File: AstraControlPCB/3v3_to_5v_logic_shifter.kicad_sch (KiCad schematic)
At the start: 16 parts, among them U6 TXB0104PWR

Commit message: Update wks file
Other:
- company: (none) -> LiveAstra Technologies
- title: 3V3 to 5V Logic Shifter -> AstraControl - Root
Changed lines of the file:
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@@
 	(paper "A4")
 	(title_block
-		(title "3V3 to 5V Logic Shifter")
+		(title "AstraControl - Root")
+		(date "2024-08-26")
+		(rev "A")
+		(company "LiveAstra Technologies")
 	)
 	(junction

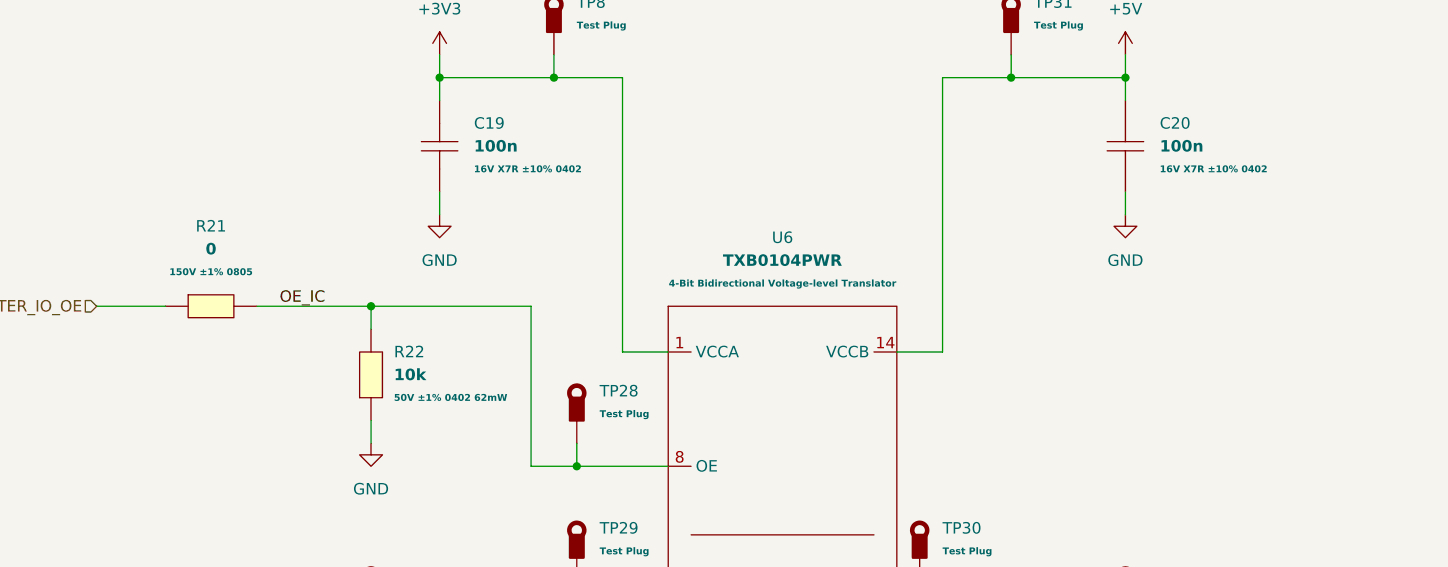
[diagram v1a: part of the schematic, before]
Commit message: Remove plus minus symbol
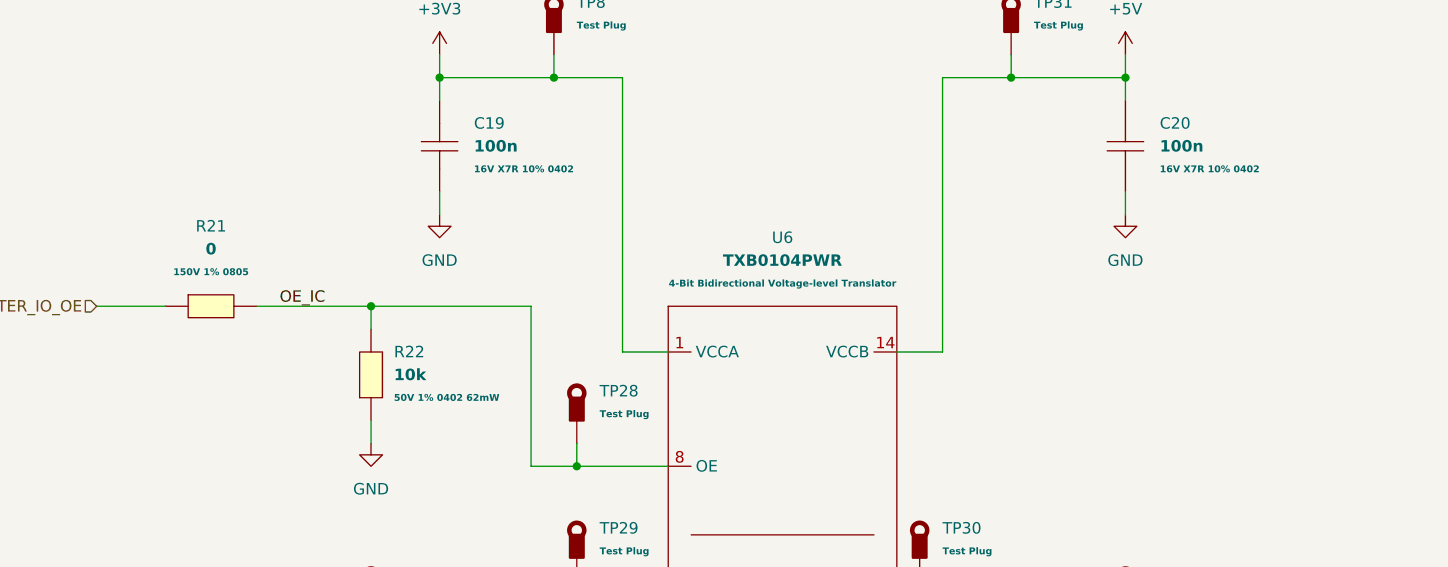
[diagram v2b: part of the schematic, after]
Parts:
- C19, C20: Extra Values 16V X7R ±10% 0402 -> 16V X7R 10% 0402
- R21: Extra Values 150V ±1% 0805 -> 150V 1% 0805
- R22: Extra Values 50V ±1% 0402 62mW -> 50V 1% 0402 62mW
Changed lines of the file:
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@@
 		(dnp no)
 		(fields_autoplaced yes)
-		(property "Reference" "#PWR059"
+		(property "Reference" "#PWR59"
 			(at 190.5 72.39 0)
 			(effects
@@
 			(project "AstraControl"
 				(path "/9a751838-dce8-4d69-8a02-736625ac74e7/0db21d8e-3390-4d67-877f-0e5d98e37848/12d48f68-9e8c-4210-a297-afac62bc105d"
-					(reference "#PWR059")
+					(reference "#PWR59")
 					(unit 1)
 				)
@@
 			)
 		)
-		(property "Extra Value" ""
-			(at 129.54 91.44 0)
-			(effects
-				(font
-					(size 1.27 1.27)
-				)
-				(hide yes)
-			)
-		)
 		(pin "1"
 		)
@@
 			)
 		)
-		(property "Extra Values" "50V ±1% 0402 62mW"
+		(property "Extra Values" "50V 1% 0402 62mW"
 			(at 109.22 86.3599 90)
 			(effects
@@
 				)
 				(justify right)
-			)
-		)
-		(property "Extra Value" ""
-			(at 106.68 83.82 0)
-			(effects
-				(font
-					(size 1.27 1.27)
-				)
-				(hide yes)
 			)
 		)
@@
 		(dnp no)
 		(fields_autoplaced yes)
-		(property "Reference" "#PWR054"
+		(property "Reference" "#PWR54"
 			(at 106.68 97.79 0)
 			(effects
@@
 			(project "AstraControl"
 				(path "/9a751838-dce8-4d69-8a02-736625ac74e7/0db21d8e-3390-4d67-877f-0e5d98e37848/12d48f68-9e8c-4210-a297-afac62bc105d"
-					(reference "#PWR054")
+					(reference "#PWR54")
 					(unit 1)
 				)
@@
 		(dnp no)
 		(fields_autoplaced yes)
-		(property "Reference" "#PWR058"
+		(property "Reference" "#PWR58"
 			(at 190.5 52.07 0)
 			(effects
@@
 			(project "AstraControl"
 				(path "/9a751838-dce8-4d69-8a02-736625ac74e7/0db21d8e-3390-4d67-877f-0e5d98e37848/12d48f68-9e8c-4210-a297-afac62bc105d"
-					(reference "#PWR058")
+					(reference "#PWR58")
 					(unit 1)
 				)
@@
 		(dnp no)
 		(fields_autoplaced yes)
-		(property "Reference" "#PWR055"
+		(property "Reference" "#PWR55"
 			(at 114.3 52.07 0)
 			(effects
@@
 			(project "AstraControl"
 				(path "/9a751838-dce8-4d69-8a02-736625ac74e7/0db21d8e-3390-4d67-877f-0e5d98e37848/12d48f68-9e8c-4210-a297-afac62bc105d"
-					(reference "#PWR055")
+					(reference "#PWR55")
 					(unit 1)
 				)
@@
 			)
 		)
-		(property "Extra Value" ""
-			(at 129.54 106.68 0)
-			(effects
-				(font
-					(size 1.27 1.27)
-				)
-				(hide yes)
-			)
-		)
 		(pin "1"
 		)
@@
 			)
 		)
-		(property "Extra Value" ""
-			(at 81.28 116.84 0)
-			(effects
-				(font
-					(size 1.27 1.27)
-				)
-				(hide yes)
-			)
-		)
 		(pin "1"
 		)
@@
 			)
 		)
-		(property "Extra Value" ""
-			(at 152.4 88.9 0)
-			(effects
-				(font
-					(size 1.27 1.27)
-				)
-				(hide yes)
-			)
-		)
 		(pin "5"
 		)
@@
 			)
 		)
-		(property "Extra Value" ""
-			(at 215.9 116.84 0)
-			(effects
-				(font
-					(size 1.27 1.27)
-				)
-				(hide yes)
-			)
-		)
 		(pin "1"
 		)
@@
 			)
 		)
-		(property "Extra Value" ""
-			(at 106.68 111.76 0)
-			(effects
-				(font
-					(size 1.27 1.27)
-				)
-				(hide yes)
-			)
-		)
 		(pin "1"
 		)
@@
 			)
 		)
-		(property "Extra Values" "150V ±1% 0805"
+		(property "Extra Values" "150V 1% 0805"
 			(at 88.9 72.39 0)
 			(effects
@@
 					(bold yes)
 				)
-			)
-		)
-		(property "Extra Value" ""
-			(at 88.9 76.2 0)
-			(effects
-				(font
-					(size 1.27 1.27)
-				)
-				(hide yes)
 			)
 		)
@@
 		(dnp no)
 		(fields_autoplaced yes)
-		(property "Reference" "#PWR056"
+		(property "Reference" "#PWR56"
 			(at 114.3 72.39 0)
 			(effects
@@
 			(project "AstraControl"
 				(path "/9a751838-dce8-4d69-8a02-736625ac74e7/0db21d8e-3390-4d67-877f-0e5d98e37848/12d48f68-9e8c-4210-a297-afac62bc105d"
-					(reference "#PWR056")
+					(reference "#PWR56")
 					(unit 1)
 				)
@@
 			)
 		)
-		(property "Extra Value" ""
-			(at 167.64 106.68 0)
-			(effects
-				(font
-					(size 1.27 1.27)
-				)
-				(hide yes)
-			)
-		)
 		(pin "1"
 		)
@@
 			)
 		)
-		(property "Extra Value" ""
-			(at 55.88 121.92 0)
-			(effects
-				(font
-					(size 1.27 1.27)
-				)
-				(hide yes)
-			)
-		)
 		(pin "1"
 		)
@@
 		(dnp no)
 		(fields_autoplaced yes)
-		(property "Reference" "#PWR057"
+		(property "Reference" "#PWR57"
 			(at 152.4 143.51 0)
 			(effects
@@
 			(project "AstraControl"
 				(path "/9a751838-dce8-4d69-8a02-736625ac74e7/0db21d8e-3390-4d67-877f-0e5d98e37848/12d48f68-9e8c-4210-a297-afac62bc105d"
-					(reference "#PWR057")
+					(reference "#PWR57")
 					(unit 1)
 				)
@@
 			)
 		)
-		(property "Extra Value" ""
-			(at 243.84 121.92 0)
-			(effects
-				(font
-					(size 1.27 1.27)
-				)
-				(hide yes)
-			)
-		)
 		(pin "1"
 		)
@@
 			)
 		)
-		(property "Extra Value" ""
-			(at 127 48.26 0)
-			(effects
-				(font
-					(size 1.27 1.27)
-				)
-				(hide yes)
-			)
-		)
 		(pin "1"
 		)
@@
 			)
 		)
-		(property "Extra Value" ""
-			(at 177.8 48.26 0)
-			(effects
-				(font
-					(size 1.27 1.27)
-				)
-				(hide yes)
-			)
-		)
 		(pin "1"
 		)
@@
 			)
 		)
-		(property "Extra Values" "16V X7R ±10% 0402"
+		(property "Extra Values" "16V X7R 10% 0402"
 			(at 118.11 60.9599 90)
 			(effects
@@
 				)
 				(justify right)
-			)
-		)
-		(property "Extra Value" ""
-			(at 114.3 58.42 0)
-			(effects
-				(font
-					(size 1.27 1.27)
-				)
-				(hide yes)
 			)
 		)
@@
 			)
 		)
-		(property "Extra Values" "16V X7R ±10% 0402"
+		(property "Extra Values" "16V X7R 10% 0402"
 			(at 194.31 60.9599 90)
 			(effects
@@
 				)
 				(justify right)
-			)
-		)
-		(property "Extra Value" ""
-			(at 190.5 58.42 0)
-			(effects
-				(font
-					(size 1.27 1.27)
-				)
-				(hide yes)
 			)
 		)
@@
 			)
 		)
-		(property "Extra Value" ""
-			(at 190.5 111.76 0)
-			(effects
-				(font
-					(size 1.27 1.27)
-				)
-				(hide yes)
-			)
-		)

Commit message: workflow
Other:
- note added: "3V3 to 5V Logic Shifter"
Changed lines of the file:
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@@
+		)
+	)
+	(text "3V3 to 5V Logic Shifter"
+		(exclude_from_sim no)
+		(at 19.05 25.4 0)
+		(effects
+			(font
+				(face "ING Me Headline")
+				(size 8 8)
+			)
+			(justify left top)
 		)
 	)
@@
 		(dnp no)
 		(fields_autoplaced yes)
-		(property "Reference" "#PWR59"
+		(property "Reference" "#PWR059"
 			(at 190.5 72.39 0)
 			(effects
@@
 			(project "AstraControl"
 				(path "/9a751838-dce8-4d69-8a02-736625ac74e7/0db21d8e-3390-4d67-877f-0e5d98e37848/12d48f68-9e8c-4210-a297-afac62bc105d"
-					(reference "#PWR59")
+					(reference "#PWR059")
 					(unit 1)
 				)
@@
 		(dnp no)
 		(fields_autoplaced yes)
-		(property "Reference" "#PWR54"
+		(property "Reference" "#PWR054"
 			(at 106.68 97.79 0)
 			(effects
@@
 			(project "AstraControl"
 				(path "/9a751838-dce8-4d69-8a02-736625ac74e7/0db21d8e-3390-4d67-877f-0e5d98e37848/12d48f68-9e8c-4210-a297-afac62bc105d"
-					(reference "#PWR54")
+					(reference "#PWR054")
 					(unit 1)
 				)
@@
 		(dnp no)
 		(fields_autoplaced yes)
-		(property "Reference" "#PWR58"
+		(property "Reference" "#PWR058"
 			(at 190.5 52.07 0)
 			(effects
@@
 			(project "AstraControl"
 				(path "/9a751838-dce8-4d69-8a02-736625ac74e7/0db21d8e-3390-4d67-877f-0e5d98e37848/12d48f68-9e8c-4210-a297-afac62bc105d"
-					(reference "#PWR58")
+					(reference "#PWR058")
 					(unit 1)
 				)
@@
 		(dnp no)
 		(fields_autoplaced yes)
-		(property "Reference" "#PWR55"
+		(property "Reference" "#PWR055"
 			(at 114.3 52.07 0)
 			(effects
@@
 			(project "AstraControl"
 				(path "/9a751838-dce8-4d69-8a02-736625ac74e7/0db21d8e-3390-4d67-877f-0e5d98e37848/12d48f68-9e8c-4210-a297-afac62bc105d"
-					(reference "#PWR55")
+					(reference "#PWR055")
 					(unit 1)
 				)
@@
 		(dnp no)
 		(fields_autoplaced yes)
-		(property "Reference" "#PWR56"
+		(property "Reference" "#PWR056"
 			(at 114.3 72.39 0)
 			(effects
@@
 			(project "AstraControl"
 				(path "/9a751838-dce8-4d69-8a02-736625ac74e7/0db21d8e-3390-4d67-877f-0e5d98e37848/12d48f68-9e8c-4210-a297-afac62bc105d"
-					(reference "#PWR56")
+					(reference "#PWR056")
 					(unit 1)
 				)
@@
 		(dnp no)
 		(fields_autoplaced yes)
-		(property "Reference" "#PWR57"
+		(property "Reference" "#PWR057"
 			(at 152.4 143.51 0)
 			(effects
@@
 			(project "AstraControl"
 				(path "/9a751838-dce8-4d69-8a02-736625ac74e7/0db21d8e-3390-4d67-877f-0e5d98e37848/12d48f68-9e8c-4210-a297-afac62bc105d"
-					(reference "#PWR57")
-					(unit 1)
-				)
+					(reference "#PWR057")
+					(unit 1)
+				)

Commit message: update
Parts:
- renumbered C19 to C20, C20 to C21, TP24 to TP22, TP25 to TP23, TP26 to TP24, TP8 to TP25, TP28 to TP26, TP29 to TP27, TP30 to TP28, TP31 to TP29, TP33 to TP30, TP34 to TP31, TP35 to TP32
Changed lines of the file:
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@@
 		(dnp no)
 		(fields_autoplaced yes)
-		(property "Reference" "#PWR059"
+		(property "Reference" "#PWR056"
 			(at 190.5 72.39 0)
 			(effects
@@
 			(project "AstraControl"
 				(path "/9a751838-dce8-4d69-8a02-736625ac74e7/0db21d8e-3390-4d67-877f-0e5d98e37848/12d48f68-9e8c-4210-a297-afac62bc105d"
-					(reference "#PWR059")
+					(reference "#PWR056")
 					(unit 1)
 				)
@@
 		(dnp no)
 		(fields_autoplaced yes)
-		(property "Reference" "TP28"
+		(property "Reference" "TP26"
 			(at 132.08 85.6276 0)
 			(effects
@@
 			(project "AstraControl"
 				(path "/9a751838-dce8-4d69-8a02-736625ac74e7/0db21d8e-3390-4d67-877f-0e5d98e37848/12d48f68-9e8c-4210-a297-afac62bc105d"
-					(reference "TP28")
+					(reference "TP26")
 					(unit 1)
 				)
@@
 		(dnp no)
 		(fields_autoplaced yes)
-		(property "Reference" "#PWR054"
+		(property "Reference" "#PWR051"
 			(at 106.68 97.79 0)
 			(effects
@@
 			(project "AstraControl"
 				(path "/9a751838-dce8-4d69-8a02-736625ac74e7/0db21d8e-3390-4d67-877f-0e5d98e37848/12d48f68-9e8c-4210-a297-afac62bc105d"
-					(reference "#PWR054")
+					(reference "#PWR051")
 					(unit 1)
 				)
@@
 		(dnp no)
 		(fields_autoplaced yes)
-		(property "Reference" "#PWR058"
+		(property "Reference" "#PWR055"
 			(at 190.5 52.07 0)
 			(effects
@@
 			(project "AstraControl"
 				(path "/9a751838-dce8-4d69-8a02-736625ac74e7/0db21d8e-3390-4d67-877f-0e5d98e37848/12d48f68-9e8c-4210-a297-afac62bc105d"
-					(reference "#PWR058")
+					(reference "#PWR055")
 					(unit 1)
 				)
@@
 		(dnp no)
 		(fields_autoplaced yes)
-		(property "Reference" "#PWR055"
+		(property "Reference" "#PWR052"
 			(at 114.3 52.07 0)
 			(effects
@@
 			(project "AstraControl"
 				(path "/9a751838-dce8-4d69-8a02-736625ac74e7/0db21d8e-3390-4d67-877f-0e5d98e37848/12d48f68-9e8c-4210-a297-afac62bc105d"
-					(reference "#PWR055")
+					(reference "#PWR052")
 					(unit 1)
 				)
@@
 		(dnp no)
 		(fields_autoplaced yes)
-		(property "Reference" "TP29"
+		(property "Reference" "TP27"
 			(at 132.08 100.8676 0)
 			(effects
@@
 			(project "AstraControl"
 				(path "/9a751838-dce8-4d69-8a02-736625ac74e7/0db21d8e-3390-4d67-877f-0e5d98e37848/12d48f68-9e8c-4210-a297-afac62bc105d"
-					(reference "TP29")
+					(reference "TP27")
 					(unit 1)
 				)
@@
 		(dnp no)
 		(fields_autoplaced yes)
-		(property "Reference" "TP25"
+		(property "Reference" "TP23"
 			(at 83.82 111.0276 0)
 			(effects
@@
 			(project "AstraControl"
 				(path "/9a751838-dce8-4d69-8a02-736625ac74e7/0db21d8e-3390-4d67-877f-0e5d98e37848/12d48f68-9e8c-4210-a297-afac62bc105d"
-					(reference "TP25")
+					(reference "TP23")
 					(unit 1)
 				)
@@
 		(dnp no)
 		(fields_autoplaced yes)
-		(property "Reference" "TP34"
+		(property "Reference" "TP31"
 			(at 218.44 111.0276 0)
 			(effects
@@
 			(project "AstraControl"
 				(path "/9a751838-dce8-4d69-8a02-736625ac74e7/0db21d8e-3390-4d67-877f-0e5d98e37848/12d48f68-9e8c-4210-a297-afac62bc105d"
-					(reference "TP34")
+					(reference "TP31")
 					(unit 1)
 				)
@@
 		(dnp no)
 		(fields_autoplaced yes)
-		(property "Reference" "TP26"
+		(property "Reference" "TP24"
 			(at 109.22 105.9476 0)
 			(effects
@@
 			(project "AstraControl"
 				(path "/9a751838-dce8-4d69-8a02-736625ac74e7/0db21d8e-3390-4d67-877f-0e5d98e37848/12d48f68-9e8c-4210-a297-afac62bc105d"
-					(reference "TP26")
+					(reference "TP24")
 					(unit 1)
 				)
@@
 		(dnp no)
 		(fields_autoplaced yes)
-		(property "Reference" "#PWR056"
+		(property "Reference" "#PWR053"
 			(at 114.3 72.39 0)
 			(effects
@@
 			(project "AstraControl"
 				(path "/9a751838-dce8-4d69-8a02-736625ac74e7/0db21d8e-3390-4d67-877f-0e5d98e37848/12d48f68-9e8c-4210-a297-afac62bc105d"
-					(reference "#PWR056")
+					(reference "#PWR053")
 					(unit 1)
 				)
@@
 		(dnp no)
 		(fields_autoplaced yes)
-		(property "Reference" "TP30"
+		(property "Reference" "TP28"
 			(at 170.18 100.8676 0)
 			(effects
@@
 			(project "AstraControl"
 				(path "/9a751838-dce8-4d69-8a02-736625ac74e7/0db21d8e-3390-4d67-877f-0e5d98e37848/12d48f68-9e8c-4210-a297-afac62bc105d"
-					(reference "TP30")
+					(reference "TP28")
 					(unit 1)
 				)
@@
 		(dnp no)
 		(fields_autoplaced yes)
-		(property "Reference" "TP24"
+		(property "Reference" "TP22"
 			(at 58.42 116.1076 0)
 			(effects
@@
 			(project "AstraControl"
 				(path "/9a751838-dce8-4d69-8a02-736625ac74e7/0db21d8e-3390-4d67-877f-0e5d98e37848/12d48f68-9e8c-4210-a297-afac62bc105d"
-					(reference "TP24")
+					(reference "TP22")
 					(unit 1)
 				)
@@
 		(dnp no)
 		(fields_autoplaced yes)
-		(property "Reference" "#PWR057"
+		(property "Reference" "#PWR054"
 			(at 152.4 143.51 0)
 			(effects
@@
 			(project "AstraControl"
 				(path "/9a751838-dce8-4d69-8a02-736625ac74e7/0db21d8e-3390-4d67-877f-0e5d98e37848/12d48f68-9e8c-4210-a297-afac62bc105d"
-					(reference "#PWR057")
+					(reference "#PWR054")
 					(unit 1)
 				)
@@
 		(dnp no)
 		(fields_autoplaced yes)
-		(property "Reference" "TP35"
+		(property "Reference" "TP32"
 			(at 246.38 116.1076 0)
 			(effects
@@
 			(project "AstraControl"
 				(path "/9a751838-dce8-4d69-8a02-736625ac74e7/0db21d8e-3390-4d67-877f-0e5d98e37848/12d48f68-9e8c-4210-a297-afac62bc105d"
-					(reference "TP35")
+					(reference "TP32")
 					(unit 1)
 				)
@@
 		(dnp no)
 		(fields_autoplaced yes)
-		(property "Reference" "TP8"
+		(property "Reference" "TP25"
 			(at 129.54 42.4476 0)
 			(effects
@@
 			(project "AstraControl"
 				(path "/9a751838-dce8-4d69-8a02-736625ac74e7/0db21d8e-3390-4d67-877f-0e5d98e37848/12d48f68-9e8c-4210-a297-afac62bc105d"
-					(reference "TP8")
+					(reference "TP25")
 					(unit 1)
 				)
@@
 		(dnp no)
 		(fields_autoplaced yes)
-		(property "Reference" "TP31"
+		(property "Reference" "TP29"
 			(at 180.34 42.4476 0)
 			(effects
@@
 			(project "AstraControl"
 				(path "/9a751838-dce8-4d69-8a02-736625ac74e7/0db21d8e-3390-4d67-877f-0e5d98e37848/12d48f68-9e8c-4210-a297-afac62bc105d"
-					(reference "TP31")
+					(reference "TP29")
 					(unit 1)
 				)
@@
 		(dnp no)
 		(fields_autoplaced yes)
-		(property "Reference" "C19"
+		(property "Reference" "C20"
 			(at 118.11 55.8799 90)
 			(effects
@@
 			(project "AstraControl"
 				(path "/9a751838-dce8-4d69-8a02-736625ac74e7/0db21d8e-3390-4d67-877f-0e5d98e37848/12d48f68-9e8c-4210-a297-afac62bc105d"
-					(reference "C19")
+					(reference "C20")
 					(unit 1)
 				)
@@
 		(dnp no)
 		(fields_autoplaced yes)
-		(property "Reference" "C20"
+		(property "Reference" "C21"
 			(at 194.31 55.8799 90)
 			(effects
@@
 			(project "AstraControl"
 				(path "/9a751838-dce8-4d69-8a02-736625ac74e7/0db21d8e-3390-4d67-877f-0e5d98e37848/12d48f68-9e8c-4210-a297-afac62bc105d"
-					(reference "C20")
+					(reference "C21")
 					(unit 1)
 				)
@@
 		(dnp no)
 		(fields_autoplaced yes)
-		(property "Reference" "TP33"
+		(property "Reference" "TP30"
 			(at 193.04 105.9476 0)
 			(effects
@@
 			(project "AstraControl"
 				(path "/9a751838-dce8-4d69-8a02-736625ac74e7/0db21d8e-3390-4d67-877f-0e5d98e37848/12d48f68-9e8c-4210-a297-afac62bc105d"
-					(reference "TP33")
-					(unit 1)
-				)
+					(reference "TP30")
+					(unit 1)
+				)

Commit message: Reroute complete
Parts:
- added C17: DNP, LiveAstra:C_0805_2012Metric_Pad1.18x1.45mm_HandSolder, symbol LiveAstra:C_DNP_0805
- added C28: DNP, LiveAstra:C_DNP_0805_2012Metric_Pad1.18x1.45mm_HandSolder, symbol LiveAstra:C_DNP_0805
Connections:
- net +3V3: now also C17.2
- net +5V: now also C28.2
- net GND: now also C17.1, C28.1
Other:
- moved on the sheet: R21

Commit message: Fixed fab layer
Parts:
- C17: footprint LiveAstra:C_0805_2012Metric_Pad1.18x1.45mm_HandSolder -> LiveAstra:C_DNP_0805_2012Metric_Pad1.18x1.45mm_HandSolder
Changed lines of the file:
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@@
 	)
 	(symbol
-		(lib_name "C_DNP_0805_1")
 		(lib_id "LiveAstra:C_DNP_0805")
 		(at 213.36 58.42 90)
@@
 			)
 		)
-		(property "Footprint" "LiveAstra:C_0805_2012Metric_Pad1.18x1.45mm_HandSolder"
+		(property "Footprint" "LiveAstra:C_DNP_0805_2012Metric_Pad1.18x1.45mm_HandSolder"
 			(at 100.33 58.42 0)
 			(effects
